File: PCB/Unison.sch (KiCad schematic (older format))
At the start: 269 parts, among them J1 USB4085-GF-A_REVA, J2 Conn_02x01, U1 ATmega32U4-AU, Y1 16MHz

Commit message: Update: 11ピンを使用し、OP-1スタイルと、5行レイアウトのキーを配置。
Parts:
- removed J2: Conn_02x01, Connector_PinHeader_2.54mm:PinHeader_2x01_P2.54mm_Vertical, symbol Connector_Generic:Conn_02x01
- removed SW_23_2, SW_32_2, SW_40_2, SW_70_2: SW_Push, ukiha:CherryMX_MidHeight_16mm_rev2_1.5u_guide, symbol Switch:SW_Push
- removed SW_24_2: SW_Push, ukiha:CherryMX_MidHeight_16mm_rev2_2u_guide, symbol Switch:SW_Push
- removed SW_25_4, SW_40_3, SW_40_4, SW_70_3, SW_80_2, SW_85_4: SW_Push, ukiha:CherryMX_MidHeight_16mm_rev2_1.25u_guide, symbol Switch:SW_Push
- removed SW_RE6: Rotary_Encoder_Switch, Rotary_Encoder:RotaryEncoder_Alps_EC11E-Switch_Vertical_H20mm, symbol Device:Rotary_Encoder_Switch
- added D101, D103, D104: D, Diode_SMD:D_SOD-123, symbol Device:D
- added SW_2B1, SW_3B1, SW_4B1, SW_5B1, SW_78_2, SW_82_2, SW_83_2, SW_87_2: SW_Push, ukiha:CherryMX_MidHeight_16mm_rev2, symbol Switch:SW_Push
- added SW_30_2, SW_35_3, SW_65_2, SW_65_3, SW_72_2, SW_73_2: SW_Push, ukiha:CherryMX_MidHeight_16mm_rev2_1.5u_guide, symbol Switch:SW_Push
- added SW_75_3: SW_Push, ukiha:CherryMX_MidHeight_16mm_rev2_2u_guide, symbol Switch:SW_Push
- added SW_90_2: SW_Push, ukiha:CherryMX_MidHeight_16mm_rev2_2U_vertical_guide, symbol Switch:SW_Push
- SW_20_2, SW_45_3: footprint ukiha:CherryMX_MidHeight_16mm_rev2_1.25u_guide -> ukiha:CherryMX_MidHeight_16mm_rev2_1.5u_guide
- SW_35_2, SW_85_2: footprint ukiha:CherryMX_MidHeight_16mm_rev2_1.25u_guide -> ukiha:CherryMX_MidHeight_16mm_rev2_2u_guide
- SW_45_2: footprint ukiha:CherryMX_MidHeight_16mm_rev2_1.5u_guide -> ukiha:CherryMX_MidHeight_16mm_rev2_2u_guide
- SW_45_4: footprint ukiha:CherryMX_MidHeight_16mm_rev2_2u_guide -> ukiha:CherryMX_MidHeight_16mm_rev2_1.5u_guide
- SW_97_2, SW_98_2: footprint ukiha:CherryMX_MidHeight_16mm_rev2_1.5u_guide -> ukiha:CherryMX_MidHeight_16mm_rev2
- renumbered SW_23_3 to SW_23_2, SW_30 to SW_30_1, SW_32_3 to SW_32_2, SW_65 to SW_65_1, SW_72 to SW_72_1, SW_73 to SW_73_1, SW_78 to SW_78_1, SW_82 to SW_82_1, SW_83 to SW_83_1, SW_87 to SW_87_1, SW_90 to SW_90_1
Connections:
- net RE6_2 is gone; now on net RE5_2: D89.2 (A)
- net RE1_1: now also D1.1 (K), SW_10_1.1, SW_10_2.1, SW_12_1.1, SW_12_2.1, SW_13_1.1, SW_13_2.1, SW_14.1, SW_15.1, SW_16.1, SW_17_1.1, SW_17_2.1, SW_18_1.1, SW_18_2.1, SW_19_1.1, SW_19_2.1; no longer D94.1 (K), SW_6.1, SW_7_1.1, SW_7_2.1, SW_8_1.1, SW_8_2.1, SW_9.1, SW_RE2.S1, SW_RE3.S1, SW_RE4.S1, SW_RE5.S1
- net RE2_2: now also D53.2 (A); no longer D100.2 (A)
- net RE3_2: now also D65.2 (A); no longer D53.2 (A)
- net RE4_2: now also D77.2 (A); no longer D65.2 (A)
- net RE5_2: no longer D77.2 (A)
- net pin1: no longer D8.1 (K)
- net pin2: no longer D100.1 (K), D89.1 (K)
- net pin3: no longer D53.1 (K)
- net pin4: no longer D65.1 (K)
- net pin5: no longer D77.1 (K)
- net RE4_1: now reaches D83.1 (K), SW_80_1.1, SW_81.1, SW_82_1.1, SW_83_1.1, SW_84.1, SW_85_1.1, SW_85_2.1, SW_85_3.1, SW_86.1, SW_87_1.1, SW_89.1
- net RE4_1: now also SW_RE4.S1, SW_82_2.1, SW_83_2.1, SW_87_2.1
- net at D14.1 (K), SW_20_1.1, SW_20_2.1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: now also SW_2B1.1
- net at D70.2 (A), SW_75_1.2, SW_75_2.2: now also SW_75_3.2
- net RE3_1: now reaches D71.1 (K), SW_70_1.1, SW_71.1, SW_72_1.1, SW_73_1.1, SW_74.1, SW_75_1.1, SW_75_2.1, SW_76.1, SW_78_1.1, SW_79.1
- net RE3_1: now also SW_RE3.S1, SW_72_2.1, SW_73_2.1, SW_75_3.1, SW_78_2.1
- net at D36.1 (K), SW_40_1.1, SW_41.1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: now also SW_4B1.1
- net at D47.1 (K), SW_50.1, SW_51.1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: now also SW_5B1.1
- net RE2_1: now reaches D59.1 (K), SW_60_1.1, SW_60_2.1, SW_61.1, SW_62.1, SW_63.1, SW_64.1, SW_65_1.1, SW_67.1, SW_68.1, SW_69.1
- net RE2_1: now also SW_RE2.S1, SW_65_2.1, SW_65_3.1
- net at D58.2 (A), SW_65_1.2: now also SW_65_2.2, SW_65_3.2
- net at D25.1 (K), SW_30_1.1, SW_31.1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: now also SW_30_2.1, SW_35_3.1, SW_3B1.1
- net at D80.2 (A), SW_83_1.2: now also SW_83_2.2
- net at D67.2 (A), SW_72_1.2: now also SW_72_2.2
- net at D73.2 (A), SW_87_1.2: now also SW_87_2.2
- net at D79.2 (A), SW_82_1.2: now also SW_82_2.2
- net at D68.2 (A), SW_73_1.2: now also SW_73_2.2
- net at D74.2 (A), SW_78_1.2: now also SW_78_2.2
- net at D35.2 (A), SW_35_1.2, SW_35_2.2: now also SW_35_3.2
- net at D30.2 (A), SW_30_1.2: now also SW_30_2.2
- net at D99.2 (A), SW_90_1.2: now also SW_90_2.2
- net RE6_1 renamed RE5_1
- net RE5_1: now also SW_RE5.S1, SW_90_2.1
- net RE6_A renamed pin11
- net pin11: now also D100.1 (K), D53.1 (K), D65.1 (K), D77.1 (K), D8.1 (K), D89.1 (K), D101.1 (K), D103.1 (K), D104.1 (K)
- net RE6_B: no longer names the net of U1.29 (PB5)
- new net: D94.1 (K), SW_6.1, SW_7_1.1, SW_7_2.1, SW_8_1.1, SW_8_2.1, SW_9.1
- new net: D100.2 (A), SW_2B1.2
- new net: D101.2 (A), SW_3B1.2
- new net: D103.2 (A), SW_4B1.2
- new net: D104.2 (A), SW_5B1.2
- no-connect marks 6 -> 7
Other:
- note added: "SW_1B"
- note added: "SW_6B"
- note added: "SW_7B"
- note added: "SW_8B"
- note added: "SW_9B"
- note removed: "SW_01"
- note removed: "SW_02"
- note removed: "SW_03"
- note removed: "SW_04"
- note removed: "SW_05"
- note removed: "SW_92"
- note removed: "SW_93\nReserve"
- moved on the sheet: D53, D65, D77, D8, D89, SW_23_2, SW_32_2

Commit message: Update: 回路図：11ピンのマトリクスから10ピンに変更。
OP-1レイアウト（4行＋最上段の1行）と5行レイアウトは排他のため、どちらも5行のマトリクスに収まる。
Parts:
- removed D100, D101, D103, D104, D53, D65, D77, D8, D89: D, Diode_SMD:D_SOD-123, symbol Device:D
- removed L14: YS_SK6812MINI_E_modify_GND_powerInput, mx2u:YS-SK6812MINI-E, symbol mx2u:YS_SK6812MINI_E_modify_GND_powerInput
- renumbered SW_36 to SW_36_1, SW_2B1 to SW_36_2, SW_41 to SW_41_1, SW_3B1 to SW_41_2, SW_46 to SW_46_1, SW_4B1 to SW_46_2, SW_51 to SW_51_1, SW_5B1 to SW_51_2
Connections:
- net RE1_1: now also D14.1 (K), SW_20_1.1, SW_20_2.1, SW_21.1, SW_23_1.1, SW_23_2.1, SW_24_1.1, SW_25_1.1, SW_25_2.1, SW_25_3.1, SW_26.1, SW_27_1.1, SW_27_2.1, SW_28_1.1, SW_28_2.1, SW_29.1; no longer D1.1 (K), SW_10_1.1, SW_10_2.1, SW_12_1.1, SW_12_2.1, SW_13_1.1, SW_13_2.1, SW_14.1, SW_15.1, SW_16.1, SW_17_1.1, SW_17_2.1, SW_18_1.1, SW_18_2.1, SW_19_1.1, SW_19_2.1
- net RE1_2: now also D15.2 (A), SW_26.2
- net RE2_2: now also D54.2 (A), SW_61.2
- net RE3_2: now also D66.2 (A), SW_71.2
- net RE4_2: now also D78.2 (A), SW_81.2
- net RE5_2: now also D90.2 (A), SW_91.2
- net at D36.1 (K), SW_40_1.1, SW_41_1.1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: now also SW_41_2.1
- net at JP_LED1.3 (B), L15.2 (Din): now also L13.2 (DOUT)
- net at D25.1 (K), SW_30_1.1, SW_30_2.1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: now also SW_36_2.1; no longer SW_41_2.1
- net at D26.2 (A), SW_36_1.2: now also SW_36_2.2
- net at D31.2 (A), SW_41_1.2: now also SW_41_2.2
- net at D37.2 (A), SW_46_1.2: now also SW_46_2.2
- net at D42.2 (A), SW_51_1.2: now also SW_51_2.2
- net pin11: no longer names the net of U1.28 (PB4)
- new net: D1.1 (K), SW_10_1.1, SW_10_2.1, SW_12_1.1, SW_12_2.1, SW_13_1.1, SW_13_2.1, SW_14.1, SW_15.1, SW_16.1, SW_17_1.1, SW_17_2.1, SW_18_1.1, SW_18_2.1, SW_19_1.1, SW_19_2.1
- no-connect marks 7 -> 8
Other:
- note removed: "Optional: OLED alternate"
- note removed: "SW_1B"
- note removed: "SW_6B"
- note removed: "SW_7B"
- note removed: "SW_8B"
- note removed: "SW_9B"
- moved on the sheet: SW_36_2, SW_41_2, SW_46_2, SW_51_2

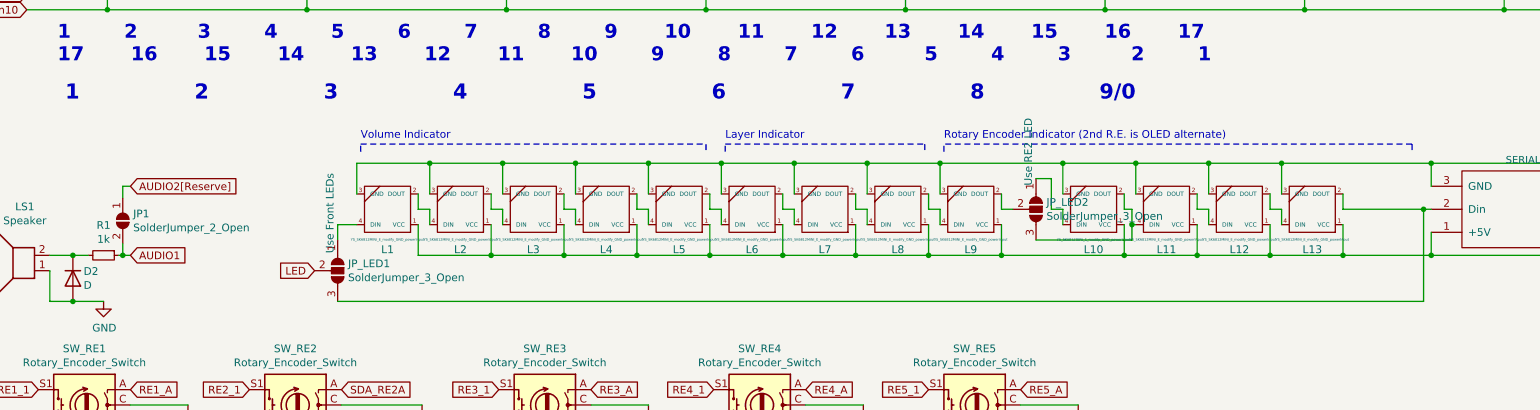
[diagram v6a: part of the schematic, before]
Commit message: Update: 回路図。LED個数、配線変更。スピーカージャンパ廃止。
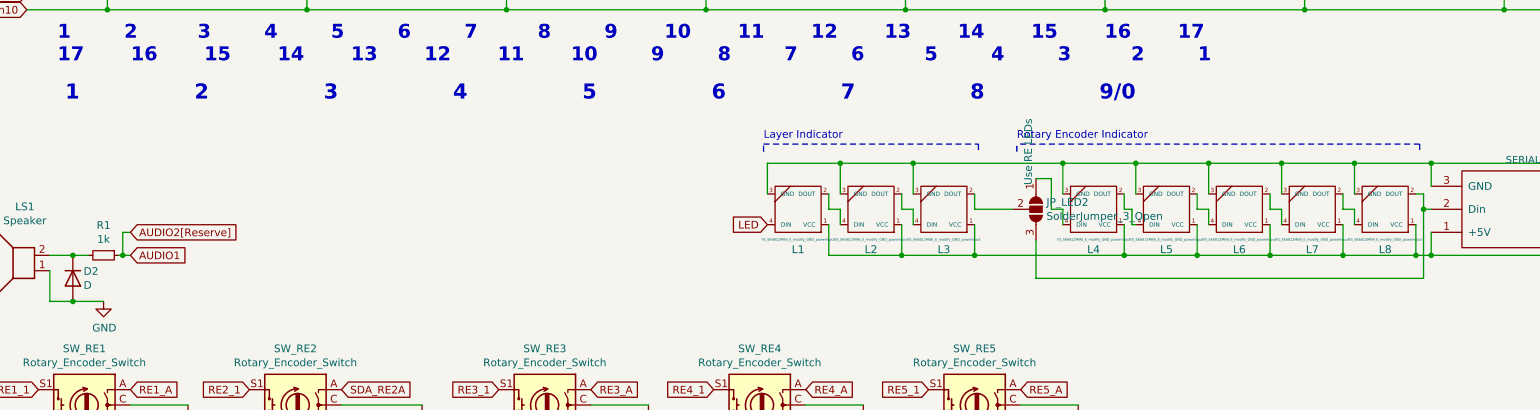
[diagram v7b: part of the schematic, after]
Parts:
- removed JP1: SolderJumper_2_Open, Jumper:SolderJumper-2_P1.3mm_Open_Pad1.0x1.5mm, symbol Jumper:SolderJumper_2_Open
- removed JP_LED1: SolderJumper_3_Open, Jumper:SolderJumper-3_P1.3mm_Open_Pad1.0x1.5mm_NumberLabels, symbol Jumper:SolderJumper_3_Open
- removed L4, L5, L6, L7, L9: YS_SK6812MINI_E_modify_GND_powerInput, mx2u:YS-SK6812MINI-E, symbol mx2u:YS_SK6812MINI_E_modify_GND_powerInput
- JP_LED2: Note Use RE2 LED -> Use RE LEDs
- renumbered L10 to L4, L11 to L5, L12 to L6, L13 to L7
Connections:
- net AUDIO2[Reserve] is gone; now on net AUDIO1: U1.31 (PC6)
- net LED: now also L1.4 (DIN)
- net at L15.2 (Din): now also JP_LED2.3 (B), L8.2 (DOUT); no longer L7.2 (DOUT)
- net at JP_LED2.2 (C): now also L3.2 (DOUT)
- net at L4.2 (DOUT), L5.4 (DIN): no longer JP_LED2.3 (B)
- net at L8.4 (DIN): now also L7.2 (DOUT)
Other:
- note added: "Rotary Encoder Indicator"
- note removed: "Rotary Encoder Indicator (2nd R.E. is OLED alternate)"
- note removed: "Volume Indicator"
- moved on the sheet: L1, L2, L3

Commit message: Update: PCB、回路図。配線完了。
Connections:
- net RE3_A: now also U1.22 (PD5); no longer U1.21 (PD3)
- net RE3_B: now also U1.25 (PD4); no longer U1.20 (PD2)
- net RE4_A: now also U1.26 (PD6); no longer U1.22 (PD5)
- net RE4_B: now also U1.27 (PD7); no longer U1.25 (PD4)
- net RE5_A: now also U1.28 (PB4); no longer U1.26 (PD6)
- net RE5_B: now also U1.29 (PB5); no longer U1.27 (PD7)
- net SCL_RE2B renamed SCL
- net SCL: no longer SW_RE2.B
- net SDA_RE2A renamed SDA
- net SDA: no longer SW_RE2.A
- new net RE2_A: SW_RE2.A, U1.20 (PD2)
- new net RE2_B: SW_RE2.B, U1.21 (PD3)
- no-connect marks 8 -> 6
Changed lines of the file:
@@
 $EndComp
 Text GLabel 15300 3325 2    50   Input ~ 0
-SCL_RE2B
+SCL
 Text GLabel 15300 3425 2    50   Input ~ 0
-SDA_RE2A
+SDA
 $Comp
 L Switch:SW_Push SW_15
@@
 Connection ~ 9100 4575
 Wire Wire Line
-	9100 4575 10400 4575
+	9100 4575 10225 4575
 Wire Wire Line
 	8050 4725 8700 4725
@@
 Text Notes 14225 3825 0    50   ~ 0
 Audio pins\nGroup1: B5, B6, B7\nGroup2: C4, C5, C6
-Text GLabel 15300 3625 2    50   Input ~ 0
+Text GLabel 15300 3825 2    50   Input ~ 0
 RE3_A
-Text GLabel 15300 3525 2    50   Input ~ 0
+Text GLabel 15300 3725 2    50   Input ~ 0
 RE3_B
-Text GLabel 15300 3825 2    50   Input ~ 0
+Text GLabel 15300 3925 2    50   Input ~ 0
 RE4_A
-Text GLabel 15300 3725 2    50   Input ~ 0
+Text GLabel 15300 4025 2    50   Input ~ 0
 RE4_B
-Text GLabel 15300 3925 2    50   Input ~ 0
+Text GLabel 15300 2525 2    50   Input ~ 0
 RE5_A
-Text GLabel 15300 4025 2    50   Input ~ 0
+Text GLabel 15300 2625 2    50   Input ~ 0
 RE5_B
 Text GLabel 4450 11000 2    50   Input ~ 0
@@
 Connection ~ 8450 7825
 Text GLabel 2825 11000 2    50   Input ~ 0
-SCL_RE2B
+RE2_B
 Text GLabel 2825 10800 2    50   Input ~ 0
-SDA_RE2A
+RE2_A
 Text GLabel 13525 9300 0    50   Input ~ 0
-SCL_RE2B
+SCL
 Text GLabel 13525 9150 0    50   Input ~ 0
-SDA_RE2A
+SDA
 Wire Notes Line
 	5575 9250 5575 9200
@@
 Text GLabel 7150 2650 1    50   Input ~ 0
 RE2_2
-NoConn ~ 15300 2625
 Wire Wire Line
 	11700 1075 11700 2425
@@
 	7150 7475 7150 7650
 Connection ~ 7150 7650
-NoConn ~ 15300 2525
 Wire Wire Line
 	2600 2650 2600 2825
@@
 Wire Wire Line
 	9825 9925 9925 9925
+Text GLabel 15300 3625 2    50   Input ~ 0
+RE2_B
+Text GLabel 15300 3525 2    50   Input ~ 0
+RE2_A
+Wire Wire Line
+	10250 4500 10225 4500
+Wire Wire Line
+	10225 4500 10225 4575
+Connection ~ 10225 4575
+Wire Wire Line
+	10225 4575 10400 4575
 $EndSCHEMATC
